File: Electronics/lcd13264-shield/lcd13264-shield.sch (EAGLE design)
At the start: 54 parts, among them J1 MICRO-SDCARD-CONNECTOR-330006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, J3 ARDUINO_R3_SHIELDUNO_R3_SHIEL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, Q1 PNP-500mA, X1 FH12-12S-1S, X2 FH12-12S-1S

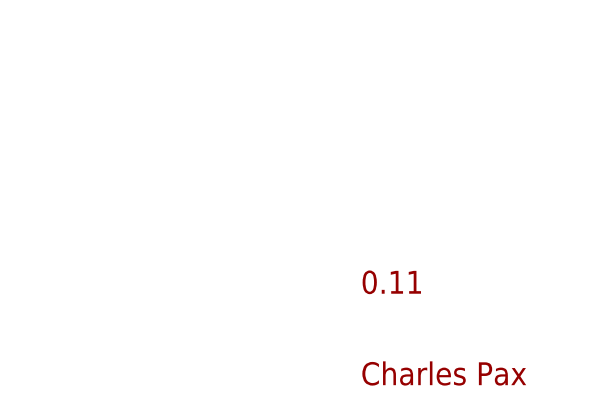
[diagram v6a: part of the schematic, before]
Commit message: Added pin function labels to top and bottom. Verified silkscreen.
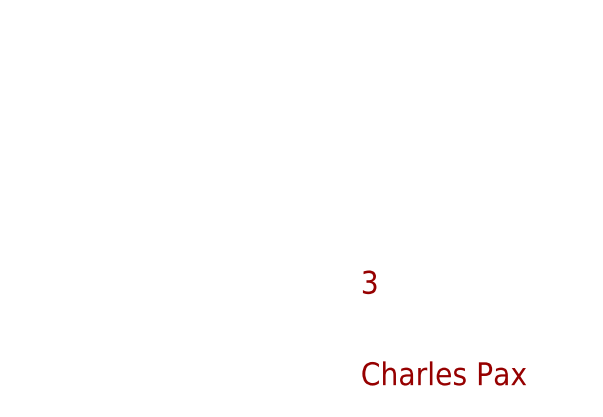
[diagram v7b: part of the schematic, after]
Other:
- note added: "3"
- note removed: "0.11"
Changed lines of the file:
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@@
 <?xml version="1.0" encoding="utf-8"?>
 <!DOCTYPE eagle SYSTEM "eagle.dtd">
-<eagle version="6.5.0">
+<eagle version="7.2.0">
 <drawing>
 <settings>
@@
 <grid distance="0.1" unitdist="inch" unit="inch" style="lines" multiple="1" display="no" altdistance="0.01" altunitdist="inch" altunit="inch"/>
 <layers>
-<layer number="1" name="Top" color="4" fill="1" visible="yes" active="no"/>
-<layer number="2" name="Route2" color="1" fill="3" visible="yes" active="no"/>
-<layer number="3" name="Route3" color="4" fill="3" visible="yes" active="no"/>
-<layer number="4" name="Route4" color="1" fill="4" visible="yes" active="no"/>
-<layer number="5" name="Route5" color="4" fill="4" visible="yes" active="no"/>
-<layer number="6" name="Route6" color="1" fill="8" visible="yes" active="no"/>
-<layer number="7" name="Route7" color="4" fill="8" visible="yes" active="no"/>
-<layer number="8" name="Route8" color="1" fill="2" visible="yes" active="no"/>
-<layer number="9" name="Route9" color="4" fill="2" visible="yes" active="no"/>
-<layer number="10" name="Route10" color="1" fill="7" visible="yes" active="no"/>
-<layer number="11" name="Route11" color="4" fill="7" visible="yes" active="no"/>
-<layer number="12" name="Route12" color="1" fill="5" visible="yes" active="no"/>
-<layer number="13" name="Route13" color="4" fill="5" visible="yes" active="no"/>
-<layer number="14" name="Route14" color="1" fill="6" visible="yes" active="no"/>
-<layer number="15" name="Route15" color="4" fill="6" visible="yes" active="no"/>
-<layer number="16" name="Bottom" color="1" fill="1" visible="yes" active="no"/>
-<layer number="17" name="Pads" color="2" fill="1" visible="yes" active="no"/>
-<layer number="18" name="Vias" color="2" fill="1" visible="yes" active="no"/>
-<layer number="19" name="Unrouted" color="6" fill="1" visible="yes" active="no"/>
-<layer number="20" name="Dimension" color="13" fill="1" visible="yes" active="no"/>
-<layer number="21" name="tPlace" color="7" fill="1" visible="yes" active="no"/>
-<layer number="22" name="bPlace" color="14" fill="1" visible="yes" active="no"/>
-<layer number="23" name="tOrigins" color="15" fill="1" visible="yes" active="no"/>
-<layer number="24" name="bOrigins" color="15" fill="1" visible="yes" active="no"/>
-<layer number="25" name="tNames" color="7" fill="1" visible="yes" active="no"/>
-<layer number="26" name="bNames" color="7" fill="1" visible="yes" active="no"/>
-<layer number="27" name="tValues" color="7" fill="1" visible="yes" active="no"/>
-<layer number="28" name="bValues" color="7" fill="1" visible="yes" active="no"/>
+<layer number="1" name="Top" color="4" fill="1" visible="no" active="no"/>
+<layer number="2" name="Route2" color="1" fill="3" visible="no" active="no"/>
+<layer number="3" name="Route3" color="4" fill="3" visible="no" active="no"/>
+<layer number="4" name="Route4" color="1" fill="4" visible="no" active="no"/>
+<layer number="5" name="Route5" color="4" fill="4" visible="no" active="no"/>
+<layer number="6" name="Route6" color="1" fill="8" visible="no" active="no"/>
+<layer number="7" name="Route7" color="4" fill="8" visible="no" active="no"/>
+<layer number="8" name="Route8" color="1" fill="2" visible="no" active="no"/>
+<layer number="9" name="Route9" color="4" fill="2" visible="no" active="no"/>
+<layer number="10" name="Route10" color="1" fill="7" visible="no" active="no"/>
+<layer number="11" name="Route11" color="4" fill="7" visible="no" active="no"/>
+<layer number="12" name="Route12" color="1" fill="5" visible="no" active="no"/>
+<layer number="13" name="Route13" color="4" fill="5" visible="no" active="no"/>
+<layer number="14" name="Route14" color="1" fill="6" visible="no" active="no"/>
+<layer number="15" name="Route15" color="4" fill="6" visible="no" active="no"/>
+<layer number="16" name="Bottom" color="1" fill="1" visible="no" active="no"/>
+<layer number="17" name="Pads" color="2" fill="1" visible="no" active="no"/>
+<layer number="18" name="Vias" color="2" fill="1" visible="no" active="no"/>
+<layer number="19" name="Unrouted" color="6" fill="1" visible="no" active="no"/>
+<layer number="20" name="Dimension" color="13" fill="1" visible="no" active="no"/>
+<layer number="21" name="tPlace" color="7" fill="1" visible="no" active="no"/>
+<layer number="22" name="bPlace" color="14" fill="1" visible="no" active="no"/>
+<layer number="23" name="tOrigins" color="15" fill="1" visible="no" active="no"/>
+<layer number="24" name="bOrigins" color="15" fill="1" visible="no" active="no"/>
+<layer number="25" name="tNames" color="7" fill="1" visible="no" active="no"/>
+<layer number="26" name="bNames" color="7" fill="1" visible="no" active="no"/>
+<layer number="27" name="tValues" color="7" fill="1" visible="no" active="no"/>
+<layer number="28" name="bValues" color="7" fill="1" visible="no" active="no"/>
 <layer number="29" name="tStop" color="7" fill="3" visible="no" active="no"/>
 <layer number="30" name="bStop" color="7" fill="6" visible="no" active="no"/>
@@
 <layer number="35" name="tGlue" color="7" fill="4" visible="no" active="no"/>
 <layer number="36" name="bGlue" color="7" fill="5" visible="no" active="no"/>
-<layer number="37" name="tTest" color="7" fill="1" visible="yes" active="no"/>
-<layer number="38" name="bTest" color="7" fill="1" visible="yes" active="no"/>
+<layer number="37" name="tTest" color="7" fill="1" visible="no" active="no"/>
+<layer number="38" name="bTest" color="7" fill="1" visible="no" active="no"/>
 <layer number="39" name="tKeepout" color="4" fill="11" visible="no" active="no"/>
 <layer number="40" name="bKeepout" color="1" fill="11" visible="no" active="no"/>
@@
 <layer number="44" name="Drills" color="7" fill="1" visible="no" active="no"/>
 <layer number="45" name="Holes" color="7" fill="1" visible="no" active="no"/>
-<layer number="46" name="Milling" color="3" fill="1" visible="yes" active="no"/>
-<layer number="47" name="Measures" color="7" fill="1" visible="yes" active="no"/>
-<layer number="48" name="Document" color="7" fill="1" visible="yes" active="no"/>
-<layer number="49" name="Reference" color="7" fill="1" visible="yes" active="no"/>
-<layer number="50" name="dxf" color="7" fill="1" visible="yes" active="no"/>
-<layer number="51" name="tDocu" color="6" fill="1" visible="yes" active="no"/>
-<layer number="52" name="bDocu" color="7" fill="1" visible="yes" active="no"/>
-<layer number="53" name="tGND_GNDA" color="7" fill="9" visible="yes" active="no"/>
-<layer number="54" name="bGND_GNDA" color="1" fill="9" visible="yes" active="no"/>
-<layer number="56" name="wert" color="7" fill="1" visible="yes" active="no"/>
-<layer number="57" name="tCAD" color="7" fill="1" visible="yes" active="no"/>
-<layer number="59" name="tCarbon" color="7" fill="1" visible="yes" active="no"/>
-<layer number="60" name="bCarbon" color="7" fill="1" visible="yes" active="no"/>
+<layer number="46" name="Milling" color="3" fill="1" visible="no" active="no"/>
+<layer number="47" name="Measures" color="7" fill="1" visible="no" active="no"/>
+<layer number="48" name="Document" color="7" fill="1" visible="no" active="no"/>
+<layer number="49" name="Reference" color="7" fill="1" visible="no" active="no"/>
+<layer number="50" name="dxf" color="7" fill="1" visible="no" active="no"/>
+<layer number="51" name="tDocu" color="6" fill="1" visible="no" active="no"/>
+<layer number="52" name="bDocu" color="7" fill="1" visible="no" active="no"/>
+<layer number="53" name="tGND_GNDA" color="7" fill="9" visible="no" active="no"/>
+<layer number="54" name="bGND_GNDA" color="1" fill="9" visible="no" active="no"/>
+<layer number="56" name="wert" color="7" fill="1" visible="no" active="no"/>
+<layer number="57" name="tCAD" color="7" fill="1" visible="no" active="no"/>
+<layer number="59" name="tCarbon" color="7" fill="1" visible="no" active="no"/>
+<layer number="60" name="bCarbon" color="7" fill="1" visible="no" active="no"/>
 <layer number="90" name="Modules" color="5" fill="1" visible="yes" active="yes"/>
 <layer number="91" name="Nets" color="2" fill="1" visible="yes" active="yes"/>
@@
 <wire x1="144.78" y1="190.5" x2="144.78" y2="254" width="0.2032" layer="94"/>
 <text x="147.32" y="248.92" size="3.81" layer="94">Buttons</text>
-<text x="330.2" y="15.24" size="2.54" layer="94" align="center-left">0.11</text>
+<text x="330.2" y="15.24" size="2.54" layer="94" align="center-left">3</text>
 <wire x1="223.52" y1="238.76" x2="281.94" y2="238.76" width="0.2032" layer="94"/>
 <wire x1="223.52" y1="238.76" x2="223.52" y2="195.58" width="0.2032" layer="94"/>

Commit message: Added MPN for LCD_BL PNP transistor.
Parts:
- Q1: MPN (none) -> MMBT3906; OC_MOUSER (none) -> 512-MMBT3906
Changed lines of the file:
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@@
 <part name="P+3" library="SparkFun" deviceset="3.3V" device=""/>
 <part name="SUPPLY3" library="SparkFun-Aesthetics" deviceset="5V" device=""/>
-<part name="Q1" library="SparkFun-DiscreteSemi" deviceset="TRANSISTOR-PNP-DDTB142TC" device="" value="PNP-500mA"/>
+<part name="Q1" library="SparkFun-DiscreteSemi" deviceset="TRANSISTOR-PNP-DDTB142TC" device="" value="PNP-500mA">
+<attribute name="MPN" value="MMBT3906"/>
+<attribute name="OC_MOUSER" value="512-MMBT3906"/>
+</part>
 <part name="P+5" library="SparkFun" deviceset="3.3V" device=""/>
 <part name="C3" library="PaxInstrument-T400" deviceset="SPARKFUN-CAPACITORS_CAP" device="0603-CAP" value="100nF">
@@
 <instance part="P+3" gate="G$1" x="261.62" y="170.18"/>
 <instance part="SUPPLY3" gate="G$1" x="266.7" y="172.72"/>
-<instance part="Q1" gate="Q1" x="170.18" y="139.7" rot="MR0"/>
+<instance part="Q1" gate="Q1" x="170.18" y="139.7" rot="MR0">
+<attribute name="MPN" x="170.18" y="139.7" size="1.778" layer="96" rot="MR0" display="off"/>
+<attribute name="OC_MOUSER" x="170.18" y="139.7" size="1.778" layer="96" rot="MR0" display="off"/>
+</instance>
 <instance part="P+5" gate="G$1" x="167.64" y="149.86"/>
 <instance part="C3" gate="G$1" x="172.72" y="170.18" smashed="yes" rot="R180">
